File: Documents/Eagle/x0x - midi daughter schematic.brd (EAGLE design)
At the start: 100 x 80 mm, 5 parts, among them IC3 74HC04N

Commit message: Fix last electronic issue
Updated few documents
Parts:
- removed DAC: MAX526CNG, maxim:DIL24-3
- removed IC3: 74HC04N, 74xx-eu:DIL14
- removed SERIAL-PARALLEL: 74HC595N, 74xx-eu:DIL16
- added U$1: MCP4922-E/P, Microchip_By_element14_Batch_1:DIP254P762X533-14
- moved OPTO-COUPLER 64.3 mm to (72.4, 34.3), turned to 90 degrees
- moved MICRO-CONTROLER 18.5 mm to (48.3, 61.0)
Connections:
- removed net AGND: DAC.5
- removed net DGND: DAC.7
- removed net N$10: MICRO-CONTROLER.C1, SERIAL-PARALLEL.11
- removed net N$11: MICRO-CONTROLER.C0, SERIAL-PARALLEL.10
- removed net N$13: DAC.22, MICRO-CONTROLER.D4
- removed net N$14: DAC.21, MICRO-CONTROLER.C3
- removed net N$15: DAC.20, MICRO-CONTROLER.D5
- removed net N$16: DAC.8, MICRO-CONTROLER.D7
- removed net N$17: DAC.18, MICRO-CONTROLER.E0
- removed net N$18: DAC.17, MICRO-CONTROLER.E1
- removed net N$5 (its old number): DAC.12, SERIAL-PARALLEL.4
- removed net N$6: DAC.11, SERIAL-PARALLEL.5
- removed net N$8: DAC.9, SERIAL-PARALLEL.7
- removed net N$9: MICRO-CONTROLER.C2, SERIAL-PARALLEL.12
- removed net VCC: IC3.14, MICRO-CONTROLER.5V, SERIAL-PARALLEL.16
- removed net VDD: DAC.23
- removed net VSS: DAC.4
- net GND: no longer IC3.7, MICRO-CONTROLER.GND, SERIAL-PARALLEL.8
- net N$1: now also MICRO-CONTROLER.B1, U$1.4; no longer DAC.16, SERIAL-PARALLEL.15
- net N$2: now also MICRO-CONTROLER.B2, U$1.5; no longer DAC.15, SERIAL-PARALLEL.1
- net N$3: now also MICRO-CONTROLER.C0, U$1.3; no longer DAC.14, SERIAL-PARALLEL.2
- net N$4: now also MICRO-CONTROLER.5V, OPTO-COUPLER.8, U$1.1, U$1.11, U$1.13; no longer DAC.13, SERIAL-PARALLEL.3
- net N$7: now also MICRO-CONTROLER.GND, OPTO-COUPLER.5, U$1.12, U$1.9; no longer DAC.10, SERIAL-PARALLEL.6
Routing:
- net N$5: track 44.5 -> 0.00 mm
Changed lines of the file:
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@@
 </autorouter>
 <elements>
-<element name="SERIAL-PARALLEL" library="74xx-eu" package="DIL16" value="74HC595N" x="57.15" y="29.21" rot="R270"/>
-<element name="DAC" library="maxim" package="DIL24-3" value="MAX526CNG" x="77.47" y="27.94" rot="R270">
-<attribute name="OC_NEWARK" value="unknown" x="30.48" y="0" size="1.778" layer="27" rot="R270" display="off"/>
-<attribute name="MPN" value="" x="30.48" y="0" size="1.778" layer="27" rot="R270" display="off"/>
-<attribute name="MF" value="" x="30.48" y="0" size="1.778" layer="27" rot="R270" display="off"/>
-<attribute name="OC_FARNELL" value="unknown" x="30.48" y="0" size="1.778" layer="27" rot="R270" display="off"/>
+<element name="OPTO-COUPLER" library="optocoupler" package="DIL08" value="6N138" x="72.39" y="34.29" rot="R90">
+<attribute name="OC_NEWARK" value="35K5294" x="100.33" y="76.2" size="1.778" layer="27" rot="R90" display="off"/>
+<attribute name="MPN" value="6N138" x="100.33" y="76.2" size="1.778" layer="27" rot="R90" display="off"/>
+<attribute name="MF" value="VISHAY/TELEFUNKEN" x="100.33" y="76.2" size="1.778" layer="27" rot="R90" display="off"/>
+<attribute name="OC_FARNELL" value="9860150" x="100.33" y="76.2" size="1.778" layer="27" rot="R90" display="off"/>
 </element>
-<element name="IC3" library="74xx-eu" package="DIL14" value="74HC04N" x="36.83" y="27.94" rot="R270"/>
-<element name="OPTO-COUPLER" library="optocoupler" package="DIL08" value="6N138" x="11.43" y="13.97">
-<attribute name="OC_NEWARK" value="35K5294" x="53.34" y="-13.97" size="1.778" layer="27" display="off"/>
-<attribute name="MPN" value="6N138" x="53.34" y="-13.97" size="1.778" layer="27" display="off"/>
-<attribute name="MF" value="VISHAY/TELEFUNKEN" x="53.34" y="-13.97" size="1.778" layer="27" display="off"/>
-<attribute name="OC_FARNELL" value="9860150" x="53.34" y="-13.97" size="1.778" layer="27" display="off"/>
+<element name="MICRO-CONTROLER" library="teensypp" package="TEENSY++" value="ARDUINO-TEENSY++" x="48.26" y="60.96"/>
+<element name="U$1" library="Microchip_By_element14_Batch_1" package="DIP254P762X533-14" value="MCP4922-E/P" x="40.64" y="22.86">
+<attribute name="PACKAGE" value="DIP-14" x="40.64" y="22.86" size="1.778" layer="27" display="off"/>
+<attribute name="OC_NEWARK" value="61K2950" x="40.64" y="22.86" size="1.778" layer="27" display="off"/>
+<attribute name="MPN" value="MCP4922-E/P" x="40.64" y="22.86" size="1.778" layer="27" display="off"/>
+<attribute name="SUPPLIER" value="Microchip" x="40.64" y="22.86" size="1.778" layer="27" display="off"/>
+<attribute name="OC_FARNELL" value="1292244" x="40.64" y="22.86" size="1.778" layer="27" display="off"/>
 </element>
-<element name="MICRO-CONTROLER" library="teensypp" package="TEENSY++" value="ARDUINO-TEENSY++" x="30.48" y="66.04"/>
 </elements>
 <signals>
 <signal name="GND">
-<contactref element="SERIAL-PARALLEL" pad="8"/>
-<contactref element="IC3" pad="7"/>
-<contactref element="MICRO-CONTROLER" pad="GND"/>
 <contactref element="MICRO-CONTROLER" pad="GRND1"/>
-<wire x1="31.75" y1="73.66" x2="6.35" y2="58.42" width="0" layer="19" extent="1-1"/>
-<wire x1="53.34" y1="20.32" x2="31.75" y2="73.66" width="0" layer="19" extent="1-1"/>
-<wire x1="33.02" y1="20.32" x2="53.34" y2="20.32" width="0" layer="19" extent="1-1"/>
-</signal>
-<signal name="VCC">
-<contactref element="SERIAL-PARALLEL" pad="16"/>
-<contactref element="IC3" pad="14"/>
-<contactref element="MICRO-CONTROLER" pad="5V"/>
-<wire x1="60.96" y1="38.1" x2="40.64" y2="35.56" width="0" layer="19" extent="1-1"/>
-<wire x1="54.61" y1="63.5" x2="60.96" y2="38.1" width="0" layer="19" extent="1-1"/>
-</signal>
-<signal name="AGND">
-<contactref element="DAC" pad="5"/>
-</signal>
-<signal name="DGND">
-<contactref element="DAC" pad="7"/>
-</signal>
-<signal name="VDD">
-<contactref element="DAC" pad="23"/>
-</signal>
-<signal name="VSS">
-<contactref element="DAC" pad="4"/>
 </signal>
 <signal name="_GND2">
@@
 </signal>
 <signal name="N$1">
-<contactref element="SERIAL-PARALLEL" pad="15"/>
-<contactref element="DAC" pad="16"/>
-<wire x1="60.96" y1="35.56" x2="81.28" y2="21.59" width="0" layer="19" extent="1-1"/>
+<contactref element="U$1" pad="4"/>
+<contactref element="MICRO-CONTROLER" pad="B1"/>
+<wire x1="33.02" y1="30.48" x2="39.37" y2="68.58" width="0" layer="19" extent="1-1"/>
 </signal>
 <signal name="N$2">
-<contactref element="SERIAL-PARALLEL" pad="1"/>
-<contactref element="DAC" pad="15"/>
-<wire x1="53.34" y1="38.1" x2="81.28" y2="19.05" width="0" layer="19" extent="1-1"/>
+<contactref element="U$1" pad="5"/>
+<contactref element="MICRO-CONTROLER" pad="B2"/>
+<wire x1="33.02" y1="27.94" x2="36.83" y2="68.58" width="0" layer="19" extent="1-1"/>
 </signal>
 <signal name="N$3">
-<contactref element="SERIAL-PARALLEL" pad="2"/>
-<contactref element="DAC" pad="14"/>
-<wire x1="53.34" y1="35.56" x2="81.28" y2="16.51" width="0" layer="19" extent="1-1"/>
+<contactref element="U$1" pad="3"/>
+<contactref element="MICRO-CONTROLER" pad="C0"/>
+<wire x1="33.02" y1="33.02" x2="54.61" y2="53.34" width="0" layer="19" extent="1-1"/>
+</signal>
+<signal name="N$5">
+<contactref element="OPTO-COUPLER" pad="6"/>
+<contactref element="MICRO-CONTROLER" pad="D2"/>
+<wire x1="68.58" y1="35.56" x2="34.29" y2="53.34" width="0" layer="19" extent="1-1"/>
 </signal>
 <signal name="N$4">
-<contactref element="SERIAL-PARALLEL" pad="3"/>
-<contactref element="DAC" pad="13"/>
-<wire x1="53.34" y1="33.02" x2="81.28" y2="13.97" width="0" layer="19" extent="1-1"/>
-</signal>
-<signal name="N$5">
-<contactref element="SERIAL-PARALLEL" pad="4"/>
-<contactref element="DAC" pad="12"/>
-<wire x1="53.34" y1="30.48" x2="73.66" y2="13.97" width="0" layer="19" extent="1-1"/>
-</signal>
-<signal name="N$6">
-<contactref element="SERIAL-PARALLEL" pad="5"/>
-<contactref element="DAC" pad="11"/>
-<wire x1="53.34" y1="27.94" x2="73.66" y2="16.51" width="0" layer="19" extent="1-1"/>
+<contactref element="U$1" pad="1"/>
+<contactref element="U$1" pad="11"/>
+<contactref element="U$1" pad="13"/>
+<contactref element="MICRO-CONTROLER" pad="5V"/>
+<contactref element="OPTO-COUPLER" pad="8"/>
+<wire x1="68.58" y1="30.48" x2="72.39" y2="58.42" width="0" layer="19" extent="1-1"/>
+<wire x1="40.64" y1="35.56" x2="68.58" y2="30.48" width="0" layer="19" extent="1-1"/>
+<wire x1="40.64" y1="30.48" x2="40.64" y2="35.56" width="0" layer="19" extent="1-1"/>
+<wire x1="33.02" y1="38.1" x2="40.64" y2="35.56" width="0" layer="19" extent="1-1"/>
 </signal>
 <signal name="N$7">
-<contactref element="SERIAL-PARALLEL" pad="6"/>
-<contactref element="DAC" pad="10"/>
-<wire x1="53.34" y1="25.4" x2="73.66" y2="19.05" width="0" layer="19" extent="1-1"/>
-</signal>
-<signal name="N$8">
-<contactref element="SERIAL-PARALLEL" pad="7"/>
-<contactref element="DAC" pad="9"/>
-<wire x1="53.34" y1="22.86" x2="73.66" y2="21.59" width="0" layer="19" extent="1-1"/>
-</signal>
-<signal name="N$9">
-<contactref element="SERIAL-PARALLEL" pad="12"/>
-<contactref element="MICRO-CONTROLER" pad="C2"/>
-<wire x1="60.96" y1="27.94" x2="41.91" y2="58.42" width="0" layer="19" extent="1-1"/>
-</signal>
-<signal name="N$10">
-<contactref element="MICRO-CONTROLER" pad="C1"/>
-<contactref element="SERIAL-PARALLEL" pad="11"/>
-<wire x1="60.96" y1="25.4" x2="39.37" y2="58.42" width="0" layer="19" extent="1-1"/>
-</signal>
-<signal name="N$11">
-<contactref element="MICRO-CONTROLER" pad="C0"/>
-<contactref element="SERIAL-PARALLEL" pad="10"/>
-<wire x1="60.96" y1="22.86" x2="36.83" y2="58.42" width="0" layer="19" extent="1-1"/>
-</signal>
-<signal name="N$12">
-<contactref element="OPTO-COUPLER" pad="6"/>
-<contactref element="MICRO-CONTROLER" pad="D2"/>
-<wire x1="16.51" y1="58.42" x2="16.51" y2="24.13" width="0.4064" layer="16"/>
-<wire x1="16.51" y1="24.13" x2="12.7" y2="24.13" width="0.4064" layer="16"/>
-<wire x1="12.7" y1="24.13" x2="12.7" y2="17.78" width="0.4064" layer="16"/>
-</signal>
-<signal name="N$13">
-<contactref element="MICRO-CONTROLER" pad="D4"/>
-<contactref element="DAC" pad="22"/>
-<wire x1="81.28" y1="36.83" x2="21.59" y2="58.42" width="0" layer="19" extent="1-1"/>
-</signal>
-<signal name="N$14">
-<contactref element="MICRO-CONTROLER" pad="C3"/>
-<contactref element="DAC" pad="21"/>
-<wire x1="81.28" y1="34.29" x2="44.45" y2="58.42" width="0" layer="19" extent="1-1"/>
-</signal>
-<signal name="N$15">
-<contactref element="MICRO-CONTROLER" pad="D5"/>
-<contactref element="DAC" pad="20"/>
-<wire x1="81.28" y1="31.75" x2="24.13" y2="58.42" width="0" layer="19" extent="1-1"/>
-</signal>
-<signal name="N$16">
-<contactref element="MICRO-CONTROLER" pad="D7"/>
-<contactref element="DAC" pad="8"/>
-<wire x1="73.66" y1="24.13" x2="29.21" y2="58.42" width="0" layer="19" extent="1-1"/>
-</signal>
-<signal name="N$17">
-<contactref element="MICRO-CONTROLER" pad="E0"/>
-<contactref element="DAC" pad="18"/>
-<wire x1="81.28" y1="26.67" x2="31.75" y2="58.42" width="0" layer="19" extent="1-1"/>
-</signal>
-<signal name="N$18">
-<contactref element="MICRO-CONTROLER" pad="E1"/>
-<contactref element="DAC" pad="17"/>
-<wire x1="81.28" y1="24.13" x2="34.29" y2="58.42" width="0" layer="19" extent="1-1"/>
+<contactref element="U$1" pad="9"/>
+<contactref element="U$1" pad="12"/>
+<contactref element="OPTO-COUPLER" pad="5"/>
+<contactref element="MICRO-CONTROLER" pad="GND"/>
+<wire x1="68.58" y1="38.1" x2="24.13" y2="53.34" width="0" layer="19" extent="1-1"/>
+<wire x1="40.64" y1="33.02" x2="68.58" y2="38.1" width="0" layer="19" extent="1-1"/>
+<wire x1="40.64" y1="25.4" x2="40.64" y2="33.02" width="0" layer="19" extent="1-1"/>
 </signal>
 </signals>

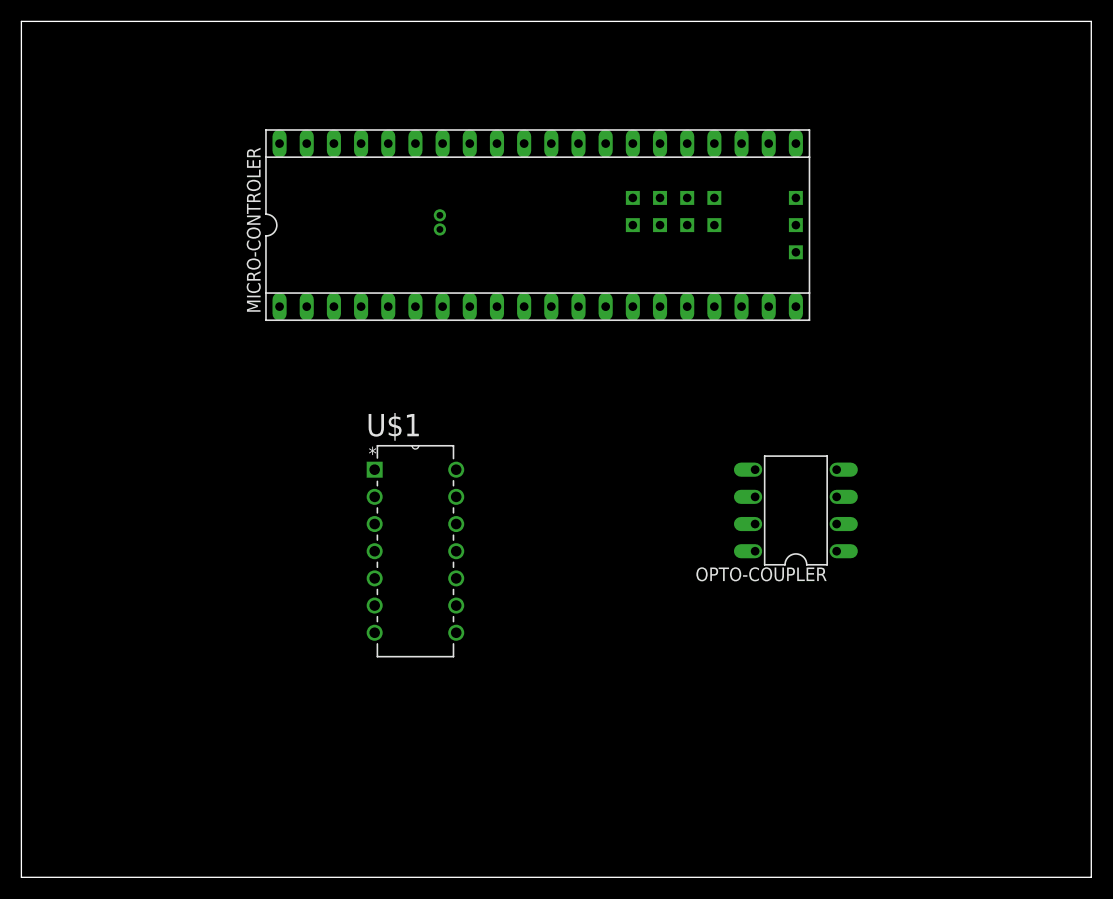
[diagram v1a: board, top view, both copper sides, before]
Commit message: Add EAGLE components
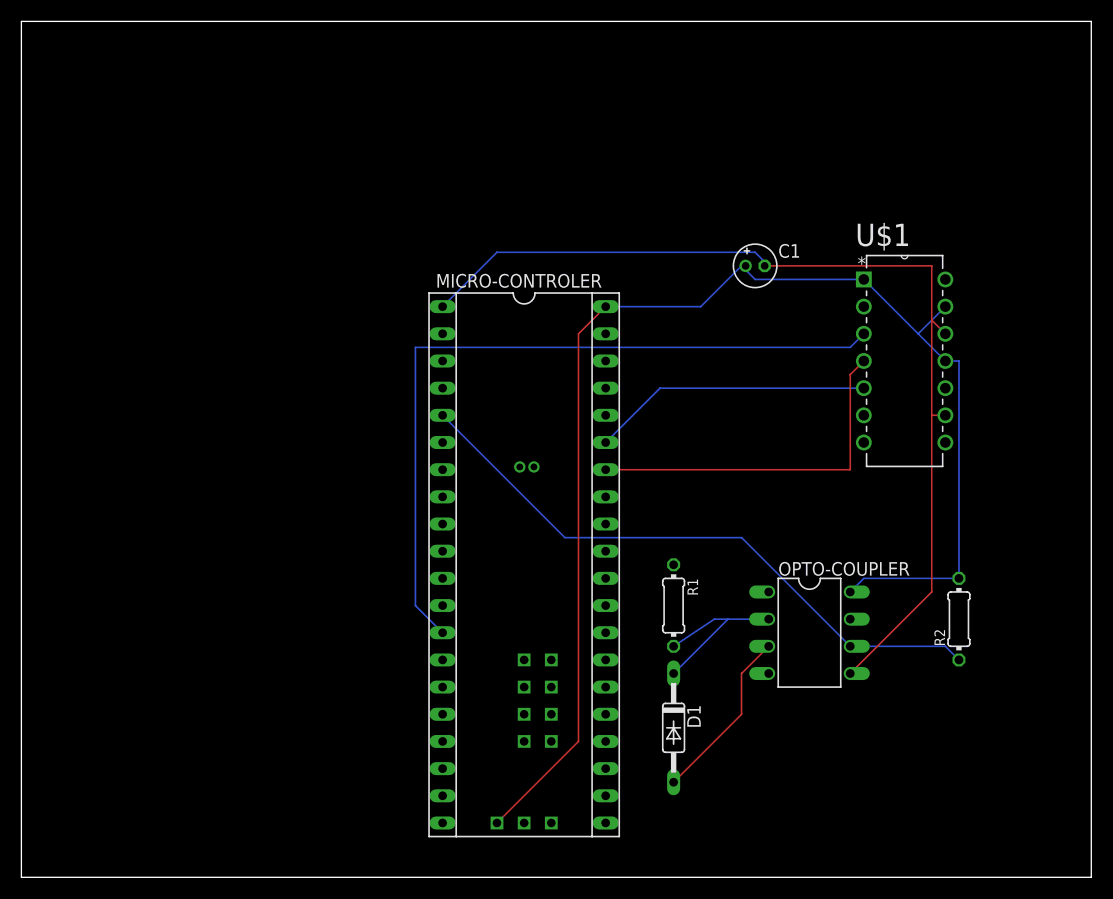
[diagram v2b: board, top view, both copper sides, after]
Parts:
- added C1: 10 µF, rcl:E1,8-4
- added D1: 1N4148DO35-10, diode:DO35-10
- added R1: 220, resistor:0204/7
- added R2: 270, resistor:0204/7
- moved U$1 49.1 mm to (86.4, 40.6)
- moved MICRO-CONTROLER 31.8 mm to (47.0, 29.2), turned to 270 degrees
- moved OPTO-COUPLER 11.5 mm to (73.7, 22.9), turned to 270 degrees
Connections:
- removed net N$7: MICRO-CONTROLER.GND, OPTO-COUPLER.5, U$1.12, U$1.9
- new net AGND: C1.-, MICRO-CONTROLER.GND, OPTO-COUPLER.5, U$1.12, U$1.9
- new net N$6: D1.C, OPTO-COUPLER.2, R1.2
- net +5V: now also C1.+, MICRO-CONTROLER.5V, OPTO-COUPLER.8, R2.2, U$1.1, U$1.11, U$1.13
- net N$4: now also D1.A, OPTO-COUPLER.3; no longer MICRO-CONTROLER.5V, OPTO-COUPLER.8, U$1.1, U$1.11, U$1.13
- net N$5: now also R2.1
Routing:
- net +5V: track 0.00 -> 125.7 mm
- net AGND: track 0.00 -> 93.4 mm
- net N$3: track 0.00 -> 70.2 mm
- net N$5: track 0.00 -> 57.7 mm
- net N$1: track 0.00 -> 33.5 mm
- net N$2: track 0.00 -> 26.2 mm
- net N$6: track 0.00 -> 16.8 mm
- net N$4: track 0.00 -> 16.4 mm
